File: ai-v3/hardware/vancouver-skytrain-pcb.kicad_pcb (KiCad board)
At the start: 2 copper layers, 150 x 150 mm, 85 parts, among them SW1 TS-1187A-B-A-B, SW2 TS-1187A-B-A-B, SW3 TS-1187A-B-A-B, SW4 TS-1187A-B-A-B, U1 XIAO-RP2040-DIP

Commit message: ai-v3: generate station labels and land/water art directly on the PCB
- export_art.py: writes station-name silkscreen and land/water shapes
  straight into the .kicad_pcb (no Inkscape/svg2shenzhen step) -
  water as F.Cu+F.Mask exposed copper (v1's technique, generated
  instead of hand-drawn), parks/islands as F.SilkS outlines only.
  Idempotent via a per-run art-manifest so re-running after editing
  vancouver.json never leaves stale/duplicate art behind.
- citymap.py: new prepared_geo() pipeline (densify/repel/clamp/
  simplify) keeps every water/land shape clear of LED pads and the
  board edge; shared by render_map.py, check_fit.py, and
  export_art.py so preview == physical board. Calibrated CHAR_W
  against KiCad's real stroke font after DRC caught label overlaps
  the simplified model had missed; added a long-name auto-shortening
  rule (display_name) and a label-vs-land collision check.
- export_art.py: per-segment safety floor for the Fraser River
  (poly_point_min_dist) - drops any rectangle still too close to an
  LED after repel rather than emit it unsafe; printed, not silent.
- Fixed real layout bugs surfaced by this: Coquitlam Central label
  ran off the board edge, Production Way's default label collided
  with it, rerouted the Fraser River off the Expo diagonal corridor.
- Verified via kicad-cli: DRC clearance/copper_edge_clearance errors
  caused by the new art are both 0; remaining categories are
  pre-existing (unrouted schematic, library footprint drift) or
  cosmetic silk warnings, documented in hardware/README.md.
- ai-v3/.gitignore: exclude VS Code's .history/ folder (nested repo,
  not project content).

Co-Authored-By: Claude Fable 5 <noreply@anthropic.com>
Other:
- board text added: "152 Street"
- board text added: "22nd Street"
- board text added: "29th Avenue"
- board text added: "Aberdeen"
- board text added: "Arbutus"
- board text added: "Bakerview"
- board text added: "Braid"
- board text added: "Brentwood Town Centre"
- board text added: "Bridgeport"
- board text added: "Broadway–City Hall"
- board text added: "Burquitlam"
- board text added: "Burrard"
- board text added: "Capstan"
- board text added: "Clayton"
- board text added: "Columbia"
- board text added: "Commercial–Broadway"
- board text added: "Coquitlam Central"
- board text added: "Edmonds"
- board text added: "Fleetwood"
- board text added: "Gateway"
- board text added: "Gilmore"
- board text added: "Granville"
- board text added: "Green Timbers"
- board text added: "Gt Northern Way"
- board text added: "Hillcrest"
- board text added: "Holdom"
- board text added: "Inlet Centre"
- board text added: "Joyce–Collingwood"
- board text added: "King Edward"
- board text added: "King George"
- board text added: "Lafarge Lake–Douglas"
- board text added: "Lake City Way"
- board text added: "Langara–49th Avenue"
- board text added: "Langley City Centre"
- board text added: "Lansdowne"
- board text added: "Lincoln"
- board text added: "Lougheed Town Centre"
- board text added: "Main St–Science World"
- board text added: "Marine Drive"
- board text added: "Metrotown"
- board text added: "Moody Centre"
- board text added: "Mount Pleasant"
- board text added: "Nanaimo"
- board text added: "New Westminster"
- board text added: "Oakridge–41st Avenue"
- board text added: "Oak–VGH"
- board text added: "Olympic Village"
- board text added: "Patterson"
- board text added: "Production Way"
- board text added: "Renfrew"
- board text added: "Richmond–Brighouse"
- board text added: "Royal Oak"
- board text added: "Rupert"
- board text added: "Sapperton"
- board text added: "Scott Road"
- board text added: "Sea Island Centre"
- board text added: "SeaBus"
- board text added: "South Granville"
- board text added: "Sperling–Burnaby Lake"
- board text added: "Stadium–Chinatown"
- board text added: "Surrey Central"
- board text added: "Templeton"
- board text added: "VCC–Clark"
- board text added: "Vancouver City Centre"
- board text added: "Waterfront"
- board text added: "Willowbrook"
- board text added: "YVR–Airport"
- board text added: "Yaletown–Roundhouse"

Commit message: ai-v3: render_board.py, redraw coastline to match real geography
- render_board.py: renders board-top.png/board-bottom.png via KiCad
  9's native 3D renderer (kicad-cli pcb render), no browser needed.
- Redrew every geo shape in vancouver.json against real Vancouver
  geography instead of the earlier coarse placeholder blobs: a
  jagged Burrard Inlet coastline with the Port Moody arm reaching
  toward Moody Centre/Inlet Centre, a proper False Creek between the
  Canada Line column and the Broadway corridor (matching where those
  stations actually sit on its two shores), Sea Island and Lulu
  Island shaped and positioned against the Fraser's arms instead of
  generic pentagons, and a Fraser South Arm along the bottom.
- citymap.py: added point_in_polygon/box_poly_overlap (proper
  concave-polygon test) - the SAT-based polys_intersect() used for
  label-vs-land collisions was invalid for the concave coastline and
  was flooding the report with false positives; replaced that one
  check only. Retuned prepared_geo()'s keepout/margin/densify
  defaults so repel() acts as a light safety net instead of visibly
  distorting the hand-drawn coastline, and widened river simplify()
  tolerance to remove small jagged render artifacts.
- Fixed real layout issues the redraw surfaced: Coquitlam
  Central/Lincoln/Lafarge shifted 3mm to fit their full names on the
  150mm board once the Port Moody notch moved, Central Park nudged
  off Patterson's label.
- Re-verified via kicad-cli: DRC clearance/copper_edge_clearance
  from the new art are still 0; rendered board-top.png/bottom.png
  confirm the coastline now reads as Vancouver, not abstract blobs.

Co-Authored-By: Claude Fable 5 <noreply@anthropic.com>
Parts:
- moved LED37 4.50 mm to (127.5, 43.5)
- moved LED38 4.50 mm to (132.0, 39.0)
- moved LED39 4.50 mm to (136.5, 34.5)

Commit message: ai-v3: draw transit lines on silkscreen, match TransLink map style
Styled after TransLink's official 'Future Rapid Transit Network' map
(user-supplied reference) - filled parks, labelled rivers/
municipalities, and future segments visually distinct from the
current network.

- export_art.py route_blocks(): every line segment as an F.SilkS
  gr_line (1.0mm). Segments touching a future station (Broadway
  Extension, Surrey-Langley Extension) render as real dashed
  segments via the new dash_points() helper.
- Found and worked around a real KiCad limitation: (stroke (type
  dash)) is an editor-only display hint - it does not survive to
  plotted/fab output (verified via both SVG export and the 3D
  renderer, both flattened it to solid). Switched to literal short
  solid segments with gaps, which do survive. Documented in
  hardware/README.md so this doesn't get rediscovered later.
- citymap.hatch_fill(): general scan-line polygon fill (even-odd
  rule, handles concave shapes), reusable for any city. Parks now
  get a 45-degree hatch fill in addition to their outline - the
  single-ink stand-in for the reference map's solid green parks.
  Lakes/islands unchanged (water fill / outline-only respectively).
- New vancouver.json annotations list + export_art
  annotation_blocks(): small F.SilkS labels for municipalities
  (Vancouver, Burnaby, Surrey, Richmond, Coquitlam) and water bodies
  (North/South Arm Fraser River, English Bay, Burrard Inlet),
  matching the reference map's place-name treatment. citymap.City
  gained an  field.
- Fixed two label collisions the new annotations introduced (Sea
  Island Centre vs. the North Arm label, Richmond-Brighouse vs. the
  RICHMOND label).
- Re-verified via kicad-cli: clearance/copper_edge_clearance from
  the new art still 0; re-rendered board-top.png/board-bottom.png
  and confirmed the dashes are actually visible this time.

Co-Authored-By: Claude Fable 5 <noreply@anthropic.com>
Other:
- board text added: "BURNABY"
- board text added: "BURRARD INLET"
- board text added: "COQUITLAM"
- board text added: "ENGLISH BAY"
- board text added: "NORTH ARM FRASER RIVER"
- board text added: "RICHMOND"
- board text added: "SOUTH ARM FRASER RIVER"
- board text added: "SURREY"
- board text added: "VANCOUVER"

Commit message: ai-v3: match geography to the official TransLink map, drop labels
- Removed the municipality/river-name annotations added last pass
  (vancouver.json annotations list now empty) per request - the
  reusable code path stays for future cities that want it.
- Redrew every geo shape by hand against TransLink's official
  Future Rapid Transit Network map (user-supplied reference), not
  invented: Point Grey now reads as its own peninsula (Pacific
  Spirit Park poking into the water, same treatment as Stanley
  Park) instead of a flat coastline retreat, False Creek is a
  longer natural hook matching its real shape, and a new Colony
  Farm Regional Park sits by the Port Moody inlet near Coquitlam
  Central/Lincoln, matching the reference.
- This is a careful by-eye match against the reference image/PDF,
  not a pixel-coordinate extraction (no such tool was used) - noted
  in hardware/README.md so it reads as a starting point for further
  correction, not a claimed exact trace.
- Re-verified via kicad-cli: clearance/copper_edge_clearance from
  the new art still 0; re-rendered board-top.png/board-bottom.png.

Co-Authored-By: Claude Fable 5 <noreply@anthropic.com>
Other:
- board text removed: "BURNABY"
- board text removed: "BURRARD INLET"
- board text removed: "COQUITLAM"
- board text removed: "ENGLISH BAY"
- board text removed: "NORTH ARM FRASER RIVER"
- board text removed: "RICHMOND"
- board text removed: "SOUTH ARM FRASER RIVER"
- board text removed: "SURREY"
- board text removed: "VANCOUVER"

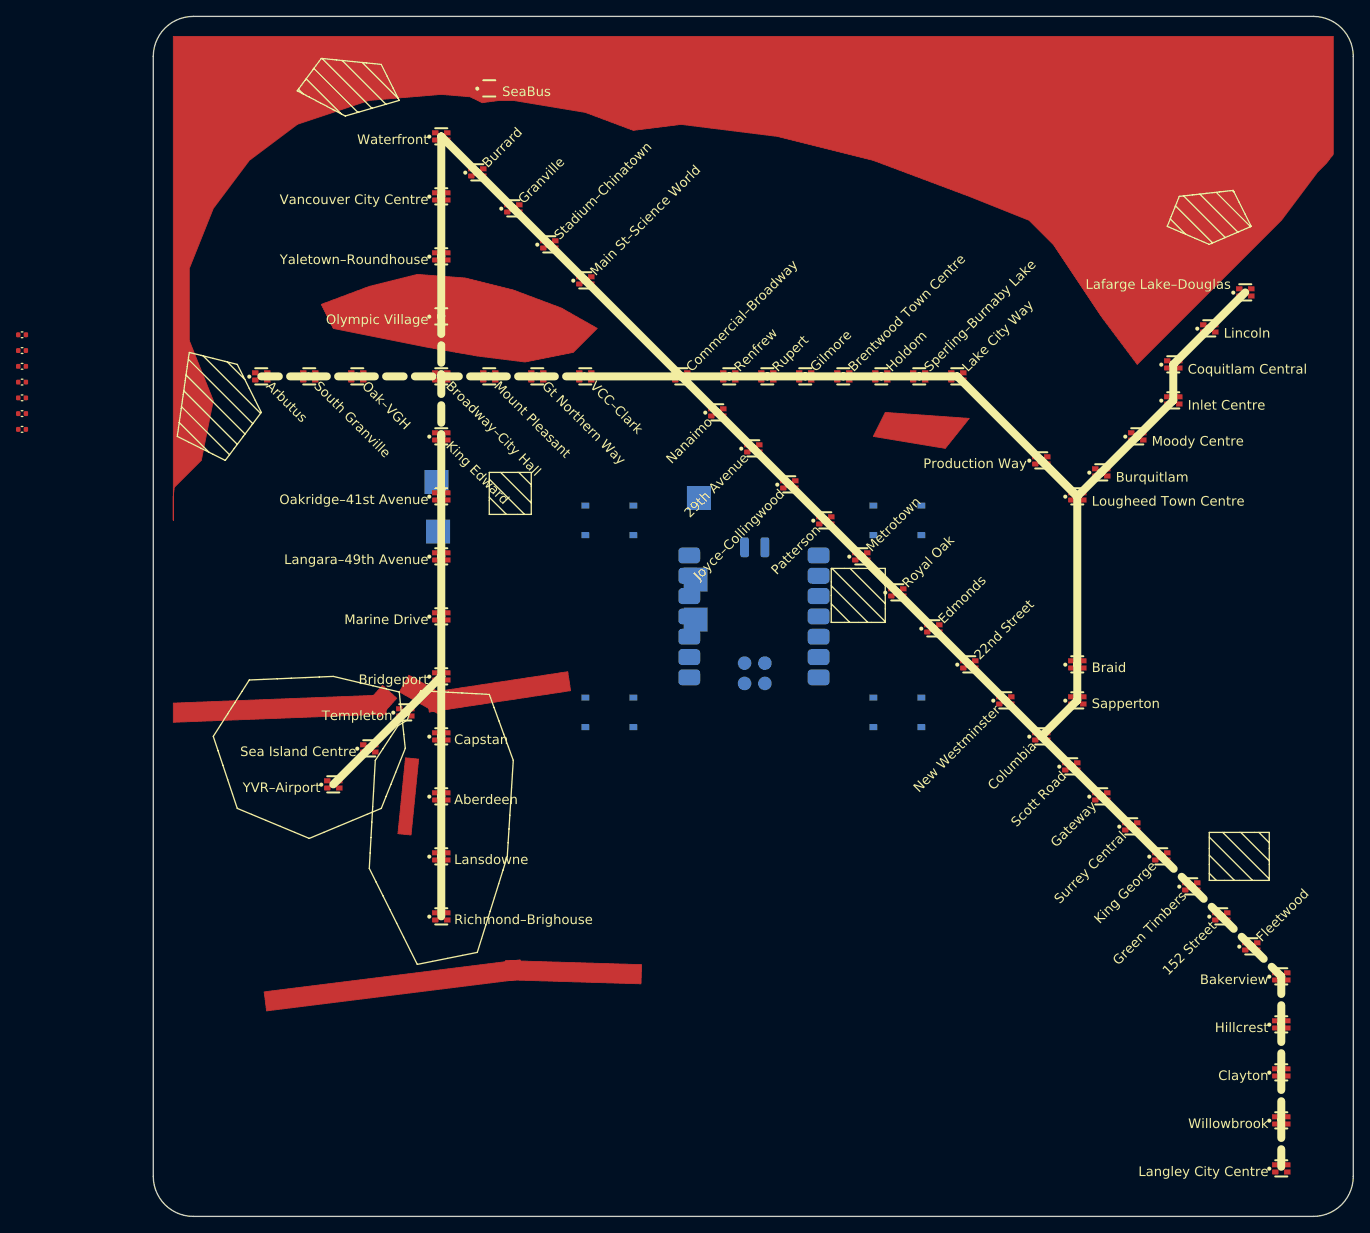
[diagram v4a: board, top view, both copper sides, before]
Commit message: ai-v3: trace station positions and geography from the real PDF map
Redoes both the station layout and land/water/park geometry from
skytrain-network-map.pdf's actual vector content instead of the
prior by-eye approximation - a real fix for the accuracy gap flagged
last round.

- input/match_stations.py: pdfplumber extracts every text label's
  exact (x,y); pymupdf extracts every station-dot circle, colour-
  coded by line (teal=Canada, blue=Expo, yellow=Millennium,
  navy=interchange/hub). Each station matched via one document-
  unique anchor word. Angled labels near line junctions
  (Commercial-Broadway, Lougheed, Sapperton, Lake City Way,
  VCC-Clark) came out garbled from pdfplumber's word-grouping on
  rotated text - resolved by hand against known real line topology
  instead (documented in input/README.md).
- input/build_geo.py: the PDF draws land as opaque polygons over a
  full-page water background - the opposite of our board. Uses
  Shapely to union all land polygons and subtract from the page
  rect; the remainder is the water, with the Fraser's arms and Sea
  Island/Lulu Island falling out as holes automatically - no river
  or island shape was hand-drawn or guessed this time. citymap.py:
  water polygons can now have holes (islands) - to_canvas_with_holes
  uses the standard bridge technique since gr_poly has no hole
  concept.
- input/build_vancouver_json.py: converts every traced PDF-point
  coordinate to the board canvas with one uniform affine transform
  (fixed margin inset + independent-axis scale for the square
  board) - preserves real proportions exactly except for that one
  deliberate aspect distortion. Broadway/Surrey-Langley extension
  stations aren't on this current-network PDF (not built yet) -
  extrapolated by continuing each real corridor's traced direction
  from its last real station.
- Softened the octilinearity check from a hard failure to a note:
  real traced positions are a few degrees off 45/90 in places, and
  that's now corr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
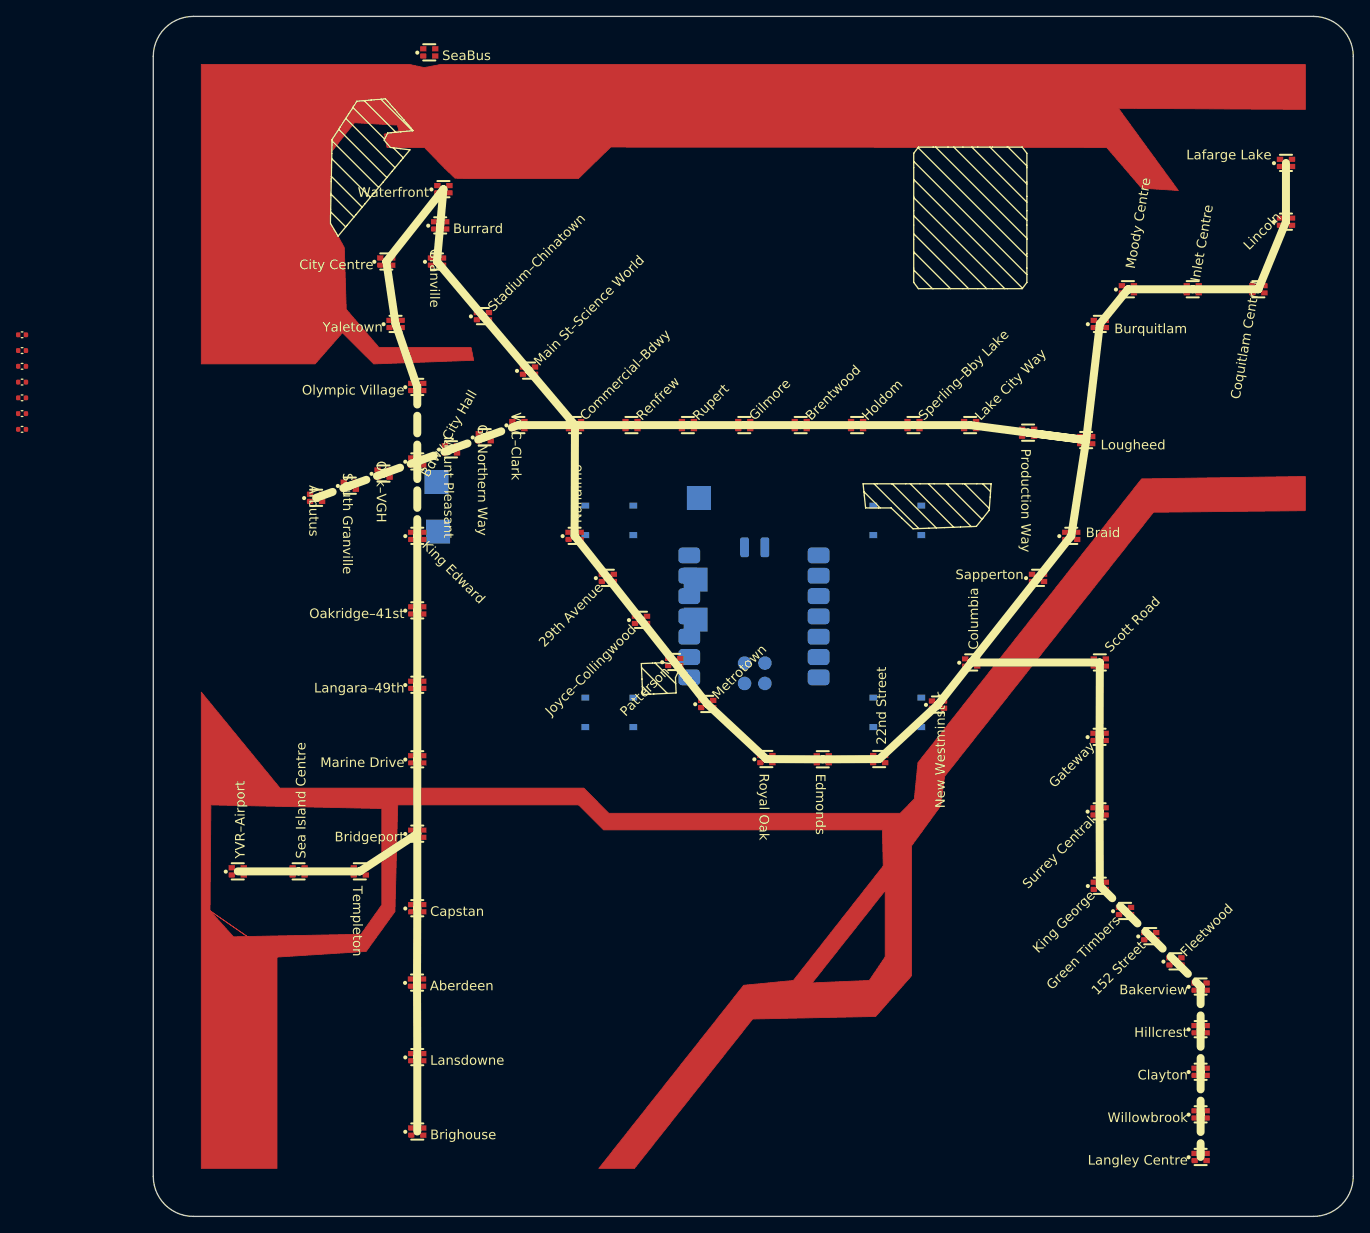
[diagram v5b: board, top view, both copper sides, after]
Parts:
- moved LED68 27.1 mm to (33.0, 139.4)
- moved LED12 26.7 mm to (69.2, 86.0)
- moved LED13 26.5 mm to (76.6, 92.8)
- moved LED11 25.9 mm to (65.1, 80.7)
- moved LED67 25.3 mm to (33.0, 130.1)
- moved LED10 25.1 mm to (61.0, 75.4)
- moved LED9 24.3 mm to (56.8, 70.2)
- moved LED8 23.6 mm to (52.7, 64.9)
- moved LED66 23.5 mm to (33.0, 120.8)
- moved LED65 21.7 mm to (33.0, 111.5)
- moved LED14 21.4 mm to (83.7, 92.9)
- moved LED62 20.7 mm to (25.8, 106.9)
- moved LED61 19.9 mm to (33.0, 102.2)
- moved LED34 18.6 mm to (118.3, 38.4)
- moved LED35 18.4 mm to (121.8, 34.1)
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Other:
- board text added: "Bdwy–City Hall"
- board text added: "Brentwood"
- board text added: "Brighouse"
- board text added: "City Centre"
- board text added: "Commercial–Bdwy"
- board text added: "Lafarge Lake"
- board text added: "Langara–49th"
- board text added: "Langley Centre"
- board text added: "Lougheed"
- board text added: "Oakridge–41st"
- board text added: "Sperling–Bby Lake"
- board text added: "Yaletown"
- board text removed: "Brentwood Town Centre"
- board text removed: "Broadway–City Hall"
- board text removed: "Commercial–Broadway"
- board text removed: "Lafarge Lake–Douglas"
- board text removed: "Langara–49th Avenue"
- board text removed: "Langley City Centre"
- board text removed: "Lougheed Town Centre"
- board text removed: "Oakridge–41st Avenue"
- board text removed: "Richmond–Brighouse"
- board text removed: "Sperling–Burnaby Lake"
- board text removed: "Vancouver City Centre"
- board text removed: "Yaletown–Roundhouse"
